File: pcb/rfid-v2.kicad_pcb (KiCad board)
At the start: 2 copper layers, 90 x 45 mm, 14 parts, among them J1 Conn_01x02_Pin, J2 Conn_01x03_Pin, J3 Conn_01x02_Pin, K1 G6S-2, Q1 PN2222A, U1 Ideaspark_ESP32_LCD_1.14", U2 RDM6300

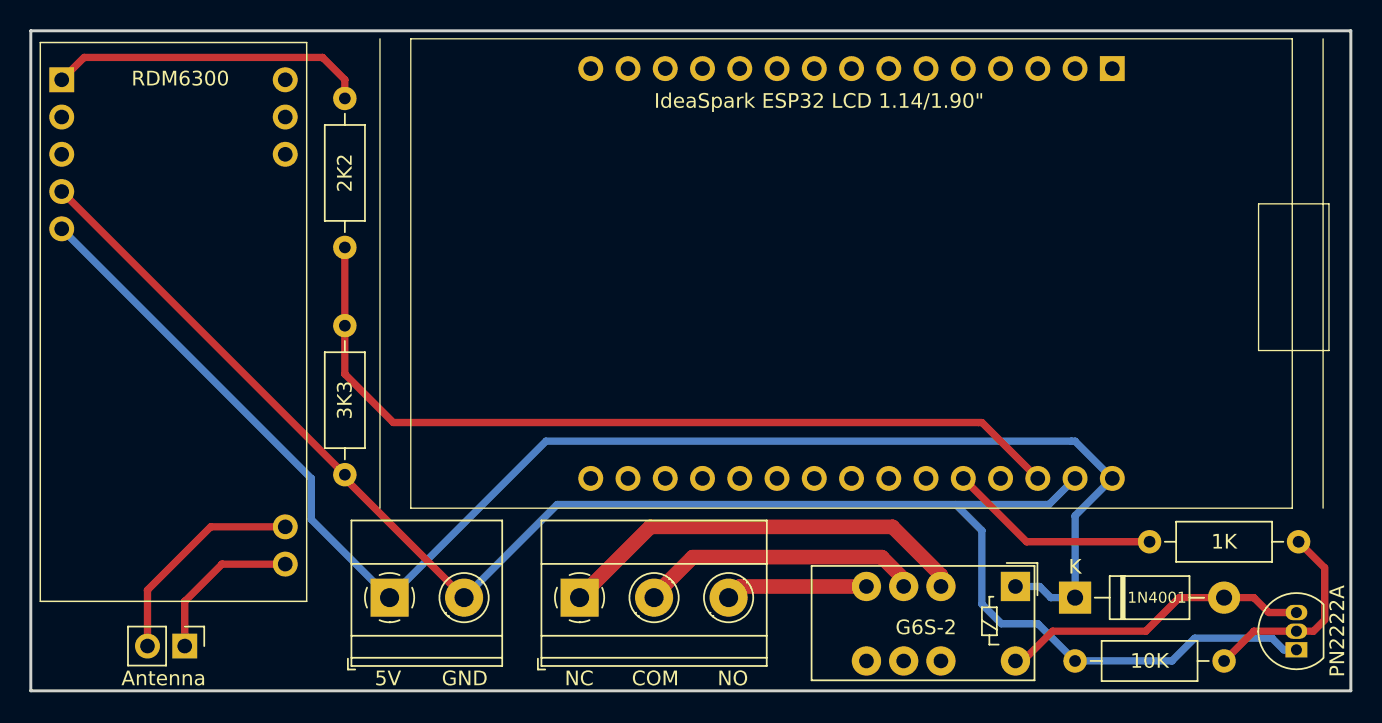
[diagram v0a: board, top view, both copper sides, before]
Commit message: pcb/code: v2a PCB
The new PCB additionally supports the TTGO/Lilygo T-display v1.1 board,
which has much better WiFi performance than the Ideaspark board.
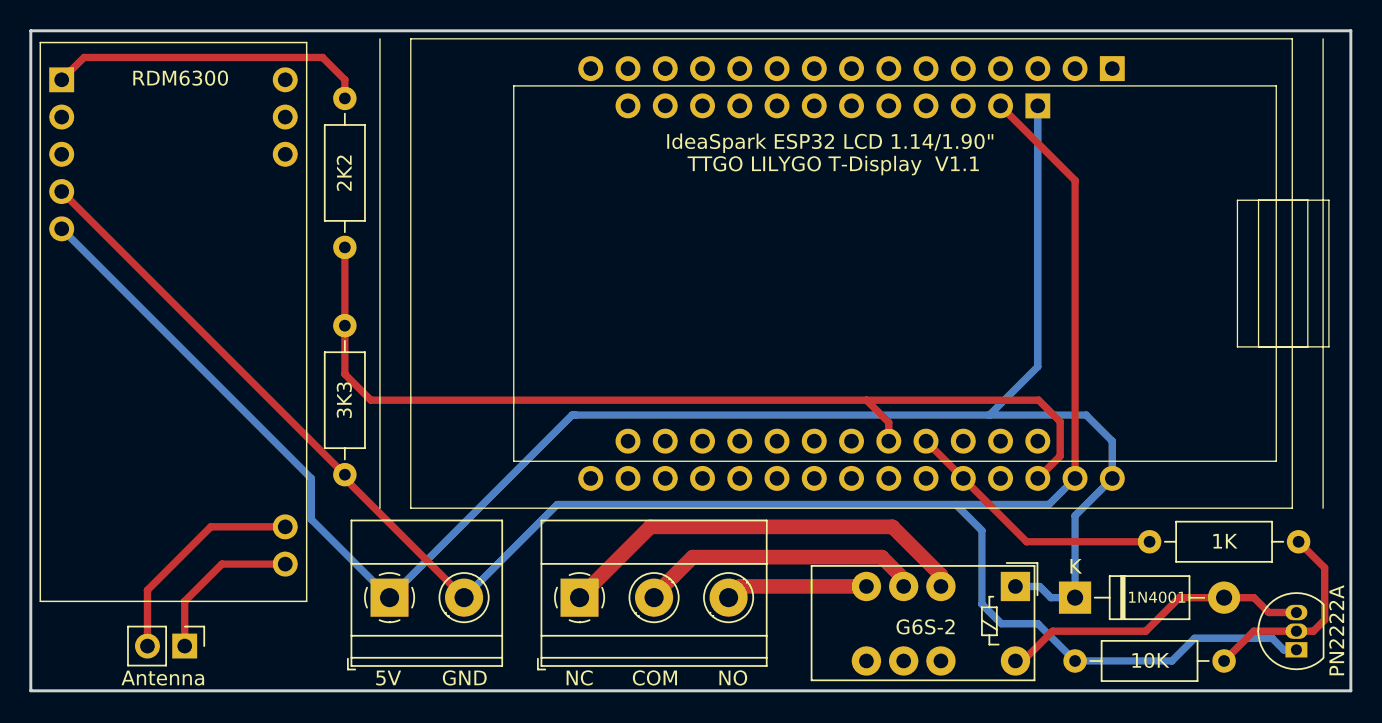
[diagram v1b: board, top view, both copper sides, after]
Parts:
- added U3: TTGO_LILYGO_T-Display_V1.1, rfid-v2:TTGO_LILYGO_T-Display_V1.1, F.Cu at (140.7, 78.0)
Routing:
- net /GND: track 116.1 -> 143.6 mm
- net /V5: track 102.7 -> 128.1 mm
- net /RFID_TX: track 58.8 -> 66.7 mm
- net /RELAY: track 14.5 -> 18.1 mm
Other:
- board text added: "FCCH RFID v2a 2026/03/15"
- board text added: "TTGO LILYGO T-Display V1.1"
- board text removed: "FCCH RFID v2 2025/01/18"
